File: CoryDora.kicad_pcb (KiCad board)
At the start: 2 copper layers, 89.6 x 60.1 mm, 26 parts, among them J1 OLED_128x32, SW1 RotaryEncoder_Switch, U1 RP2040_Zero

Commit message: chore: made modifications for v1.1
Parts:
- added G***: LOGO, DEKU_logo:DEKU_logo, B.Cu at (158.9, 116.1)
- moved SW1 1.60 mm to (147.3, 133.1)
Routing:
- net ENCODER_SW: track 43.3 -> 49.9 mm
- net ENCODER_A: track 36.9 -> 38.6 mm
- net GND: track 63.1 -> 64.7 mm
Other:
- board text added: "CoryDora v1.1"
- board text added: "S8"
- board text removed: "CoryDora v1"

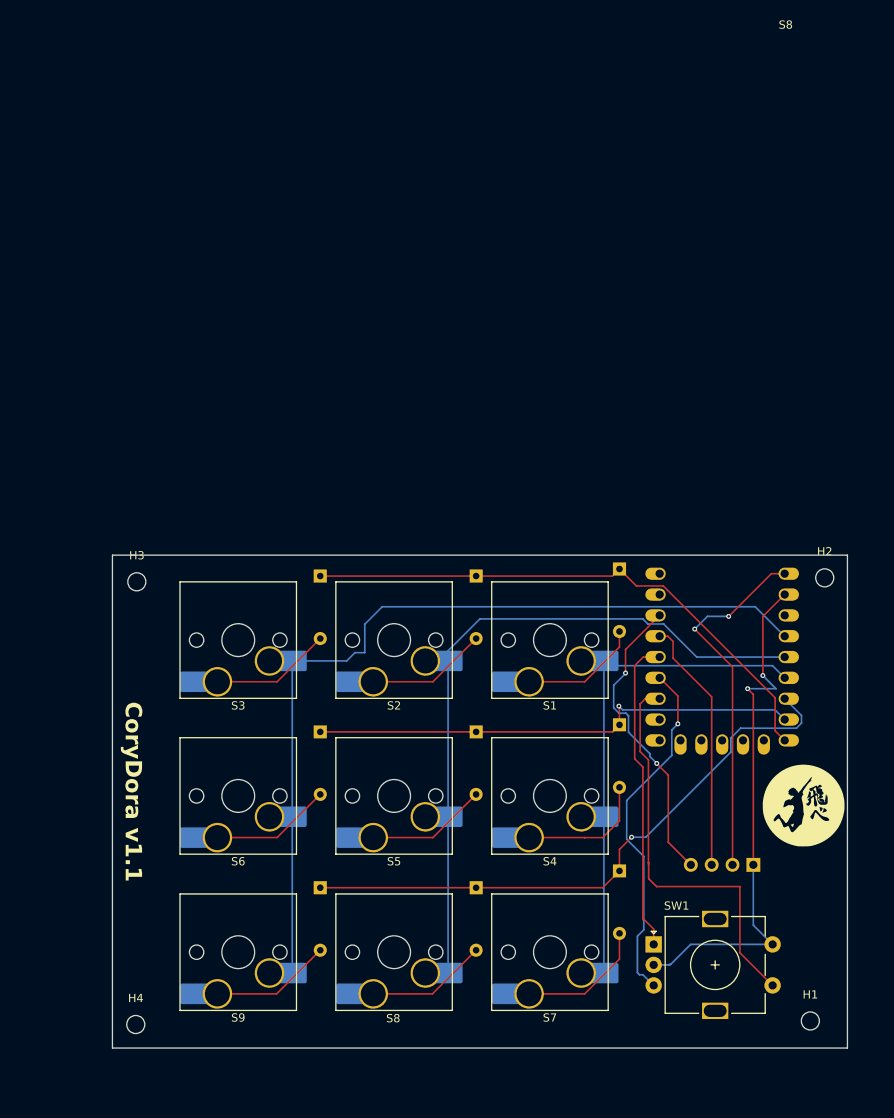
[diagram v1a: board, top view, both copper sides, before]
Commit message: chore: added front and bottom copper fill
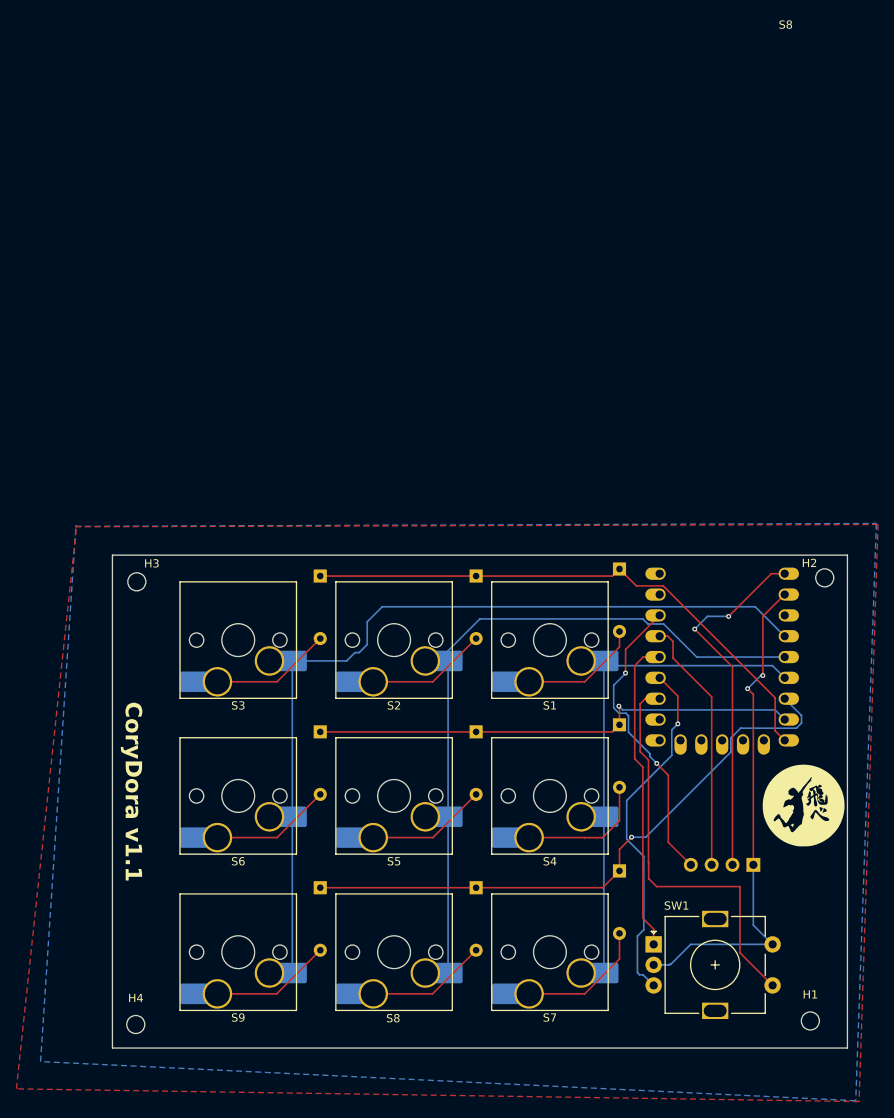
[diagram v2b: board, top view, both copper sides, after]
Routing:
- net GND: track 64.7 -> 61.5 mm
- added copper zone on B.Cu, net (none)
- added copper zone on F.Cu, net (none)
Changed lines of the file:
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@@
 			(psnegative no)
 			(psa4output no)
-			(plotreference yes)
+			(plotreference no)
 			(plotvalue no)
 			(plotfptext yes)
 			(plotinvisibletext no)
 			(sketchpadsonfab no)
-			(subtractmaskfromsilk yes)
+			(subtractmaskfromsilk no)
 			(outputformat 1)
 			(mirror no)
@@
 	(net 21 "ENCODER_B")
 	(net 22 "ENCODER_SW")
-	(net 23 "unconnected-(U1-7-Pad8)")
-	(net 24 "unconnected-(U1-12-Pad13)")
-	(net 25 "unconnected-(U1-13-Pad14)")
-	(net 26 "unconnected-(U1-0-Pad1)")
-	(net 27 "unconnected-(U1-10-Pad11)")
-	(net 28 "unconnected-(U1-11-Pad12)")
-	(net 29 "unconnected-(U1-1-Pad2)")
-	(net 30 "unconnected-(U1-3V3-Pad21)")
-	(net 31 "unconnected-(U1-8-Pad9)")
-	(net 32 "unconnected-(U1-9-Pad10)")
+	(net 23 "unconnected-(U1-9-Pad10)")
+	(net 24 "unconnected-(U1-8-Pad9)")
+	(net 25 "unconnected-(U1-3V3-Pad21)")
+	(net 26 "unconnected-(U1-1-Pad2)")
+	(net 27 "unconnected-(U1-11-Pad12)")
+	(net 28 "unconnected-(U1-10-Pad11)")
+	(net 29 "unconnected-(U1-0-Pad1)")
+	(net 30 "unconnected-(U1-13-Pad14)")
+	(net 31 "unconnected-(U1-12-Pad13)")
+	(net 32 "unconnected-(U1-7-Pad8)")
 	(footprint "Downloads:12"
 		(layer "F.Cu")
@@
 			)
 		)
+		(model "${MY_LIBRARY}/11mm-metal-shaft-rotary-encoders-tht-vertical-w-push-on-switch-1.snapshot.2/models3d/Encoders/EC11-THT-15F-green.step"
+			(offset
+				(xyz 7.5 -2.5 -0.25)
+			)
+			(scale
+				(xyz 1 1 1)
+			)
+			(rotate
+				(xyz 180 180 -90)
+			)
+		)
 	)
 	(footprint "ScottoKeebs_Hotswap:Hotswap_MX_Plated_1.00u"
@@
 		(tags "mounting hole 2.2mm no annular m2")
 		(property "Reference" "H3"
-			(at 0 -3.2 0)
+			(at 1.8288 -2.2098 0)
 			(layer "F.SilkS")
 			(effects
@@
 			(at 5.75 5.75 -90)
 			(layer "F.Fab")
-			(hide yes)
 			(effects
 				(font
@@
 		(tags "mounting hole 2.2mm no annular m2")
 		(property "Reference" "H2"
-			(at 0 -3.2 0)
+			(at -1.8542 -1.778 0)
 			(layer "F.SilkS")
 			(effects
@@
 		)
 		(property "Value" "RP2040_Zero"
-			(at -16.8434 5.54718 180)
+			(at -10.344 1.349891 -90)
 			(layer "B.SilkS")
-			(hide yes)
 			(effects
 				(font
@@
 			(layers "*.Cu" "*.Mask")
 			(remove_unused_layers no)
-			(net 26 "unconnected-(U1-0-Pad1)")
+			(net 29 "unconnected-(U1-0-Pad1)")
 			(pinfunction "0")
 			(pintype "bidirectional+no_connect")
@@
 			(layers "*.Cu" "*.Mask")
 			(remove_unused_layers no)
-			(net 29 "unconnected-(U1-1-Pad2)")
+			(net 26 "unconnected-(U1-1-Pad2)")
 			(pinfunction "1")
 			(pintype "bidirectional+no_connect")
@@
 			(layers "*.Cu" "*.Mask")
 			(remove_unused_layers no)
-			(net 23 "unconnected-(U1-7-Pad8)")
+			(net 32 "unconnected-(U1-7-Pad8)")
 			(pinfunction "7")
 			(pintype "bidirectional+no_connect")
@@
 			(layers "*.Cu" "*.Mask")
 			(remove_unused_layers no)
-			(net 31 "unconnected-(U1-8-Pad9)")
+			(net 24 "unconnected-(U1-8-Pad9)")
 			(pinfunction "8")
 			(pintype "bidirectional+no_connect")
@@
 			(layers "*.Cu" "*.Mask")
 			(remove_unused_layers no)
-			(net 32 "unconnected-(U1-9-Pad10)")
+			(net 23 "unconnected-(U1-9-Pad10)")
 			(pinfunction "9")
 			(pintype "bidirectional+no_connect")
@@
 			(layers "*.Cu" "*.Mask")
 			(remove_unused_layers no)
-			(net 27 "unconnected-(U1-10-Pad11)")
+			(net 28 "unconnected-(U1-10-Pad11)")
 			(pinfunction "10")
 			(pintype "bidirectional+no_connect")
@@
 			(layers "*.Cu" "*.Mask")
 			(remove_unused_layers no)
-			(net 28 "unconnected-(U1-11-Pad12)")
+			(net 27 "unconnected-(U1-11-Pad12)")
 			(pinfunction "11")
 			(pintype "bidirectional+no_connect")
@@
 			(layers "*.Cu" "*.Mask")
 			(remove_unused_layers no)
-			(net 24 "unconnected-(U1-12-Pad13)")
+			(net 31 "unconnected-(U1-12-Pad13)")
 			(pinfunction "12")
 			(pintype "bidirectional+no_connect")
@@
 			(layers "*.Cu" "*.Mask")
 			(remove_unused_layers no)
-			(net 25 "unconnected-(U1-13-Pad14)")
+			(net 30 "unconnected-(U1-13-Pad14)")
 			(pinfunction "13")
 			(pintype "bidirectional+no_connect")
@@
 			(layers "*.Cu" "*.Mask")
 			(remove_unused_layers no)
-			(net 30 "unconnected-(U1-3V3-Pad21)")
+			(net 25 "unconnected-(U1-3V3-Pad21)")
 			(pinfunction "3V3")
 			(pintype "power_out+no_connect")
@@
 	)
 	(segment
-		(start 162.2044 101.904262)
-		(end 160.6042 100.304062)
-		(width 0.2)
-		(layer "B.Cu")
-		(net 16)
-	)
-	(segment
-		(start 158.75 101.904262)
-		(end 162.2044 101.904262)
+		(start 160.6042 100.304062)
+		(end 160.3502 100.304062)
 		(width 0.2)
 		(layer "B.Cu")
@@
 	)
 	(segment
+		(start 160.3502 100.304062)
+		(end 158.75 101.904262)
+		(width 0.2)
+		(layer "B.Cu")
+		(net 16)
+	)
+	(segment
 		(start 149.15 135.583462)
 		(end 147.2934 135.583462)
@@
 	)
 	(segment
-		(start 114.203309 91.917153)
-		(end 159.675 91.917153)
+		(start 112.3696 93.750862)
+		(end 112.3696 96.519462)
 		(width 0.2)
 		(layer "B.Cu")
@@
 	)
 	(segment
-		(start 159.675 91.917153)
-		(end 163.265 95.507153)
+		(start 103.23 117.523262)
+		(end 103.23 136.573262)
 		(width 0.2)
 		(layer "B.Cu")
@@
 	)
 	(segment
-		(start 112.0648 94.055662)
-		(end 114.203309 91.917153)
+		(start 103.23 98.523262)
+		(end 109.8578 98.523262)
+		(width 0.2)
+		(layer "B.Cu")
+		(net 19)
+	)
+	(segment
+		(start 114.203309 91.917153)
+		(end 159.675 91.917153)
 		(width 0.2)
 		(layer "B.Cu")
@@
 	)
 	(segment
-		(start 103.23 117.523262)
-		(end 103.23 136.573262)
+		(start 112.3696 96.519462)
+		(end 111.379 97.510062)
 		(width 0.2)
 		(layer "B.Cu")
@@
 	)
 	(segment
-		(start 110.871 97.510062)
-		(end 112.0648 97.510062)
+		(start 159.675 91.917153)
+		(end 163.265 95.507153)
 		(width 0.2)
 		(layer "B.Cu")
@@
 	)
 	(segment
-		(start 103.23 98.523262)
-		(end 109.8578 98.523262)
+		(start 110.871 97.510062)
+		(end 111.379 97.510062)
 		(width 0.2)
 		(layer "B.Cu")
@@
 	)
 	(segment
-		(start 112.0648 97.510062)
-		(end 112.0648 94.055662)
+		(start 112.3696 93.750862)
+		(end 114.203309 91.917153)
 		(width 0.2)
 		(layer "B.Cu")
@@
 	)
 	(segment
-		(start 145.975 130.063262)
+		(start 147.2934 131.213462)
 		(end 145.975 129.895062)
 		(width 0.2)
@@
 	)
 	(segment
-		(start 145.975 129.895062)
-		(end 147.2934 131.213462)
-		(width 0.2)
-		(layer "F.Cu")
-		(net 20)
-	)
-	(segment
 		(start 145.975 111.455862)
 		(end 144.9832 110.464062)
@@
 	)
 	(segment
-		(start 146.685 123.113262)
-		(end 146.6596 123.087862)
-		(width 0.2)
-		(layer "F.Cu")
-		(net 22)
-	)
-	(segment
 		(start 146.274909 103.127153)
 		(end 148.025 103.127153)
@@
 	)
 	(segment
-		(start 157.8102 126.034262)
-		(end 147.6502 126.034262)
+		(start 146.685 123.113262)
+		(end 146.6596 123.087862)
 		(width 0.2)
 		(layer "F.Cu")
@@
 	)
 	(segment
-		(start 146.6596 123.347862)
-		(end 146.6596 123.087862)
+		(start 157.8102 126.034262)
+		(end 147.6502 126.034262)
 		(width 0.2)
 		(layer "F.Cu")
@@
 		(net 22)
 	)
+	(zone
+		(net 0)
+		(net_name "")
+		(layer "F.Cu")
+		(hatch edge 0.5)
+		(connect_pads
+			(clearance 0.5)
+		)
+		(min_thickness 0.25)
+		(filled_areas_thickness no)
+		(fill yes
+			(thermal_gap 0.5)
+			(thermal_bridge_width 0.5)
+			(island_removal_mode 1)
+			(island_area_min 10)
+		)
+		(polygon
+			(pts
+				(xy 76.7588 82.168462) (xy 174.6504 81.889062) (xy 172.339 152.247062) (xy 69.596 150.697662) (xy 76.9366 82.066862)
+			)
+		)
+	)
+	(zone
+		(net 0)
+		(net_name "")
+		(layer "B.Cu")
+		(hatch edge 0.5)
+		(priority 1)
+		(connect_pads
+			(clearance 0.5)
+		)
+		(min_thickness 0.25)
+		(filled_areas_thickness no)
+		(fill yes
+			(thermal_gap 0.5)
+			(thermal_bridge_width 0.5)
+			(island_removal_mode 1)
+			(island_area_min 10)
+		)
+		(polygon
+			(pts
+				(xy 76.8096 82.117662) (xy 174.4472 81.762062) (xy 171.9326 152.145462) (xy 72.5424 147.370262)
+				(xy 76.8604 81.990662)
+			)
+		)
+	)
 )

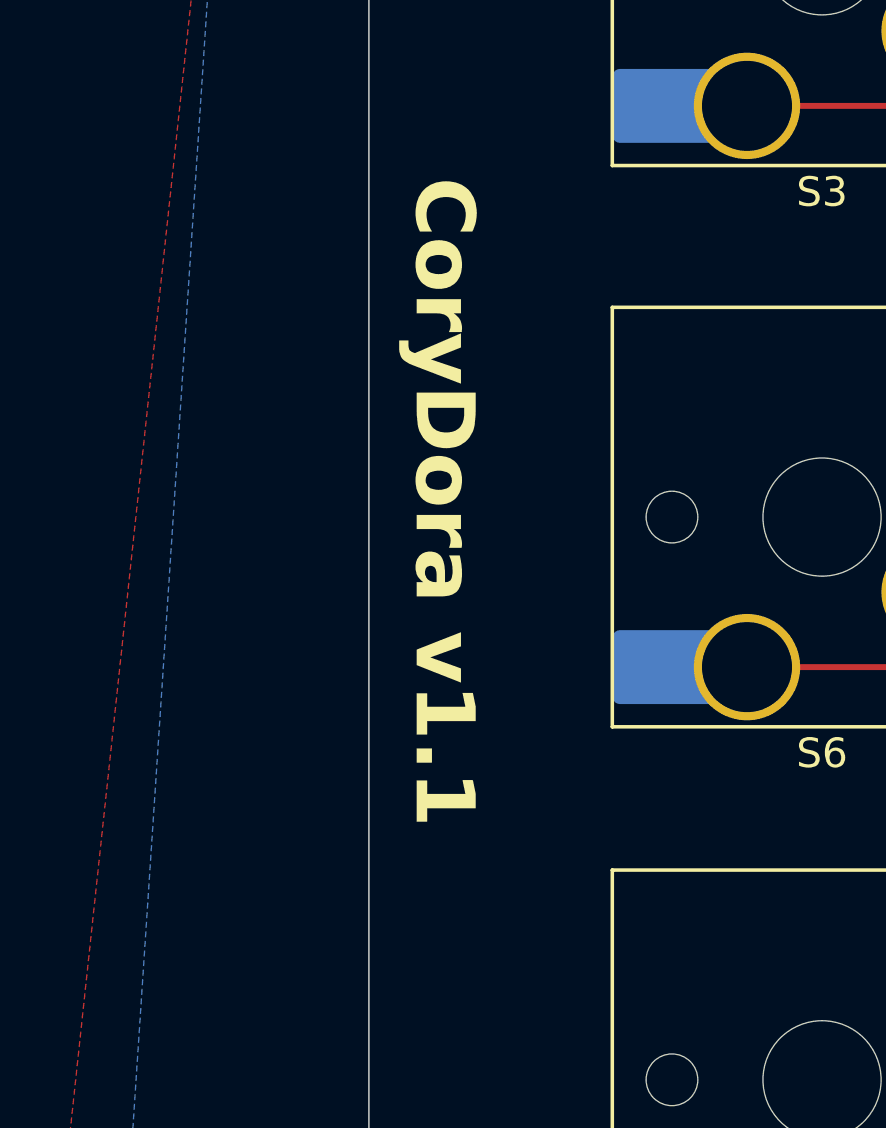
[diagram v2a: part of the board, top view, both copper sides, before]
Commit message: feat: added v1.2 case design
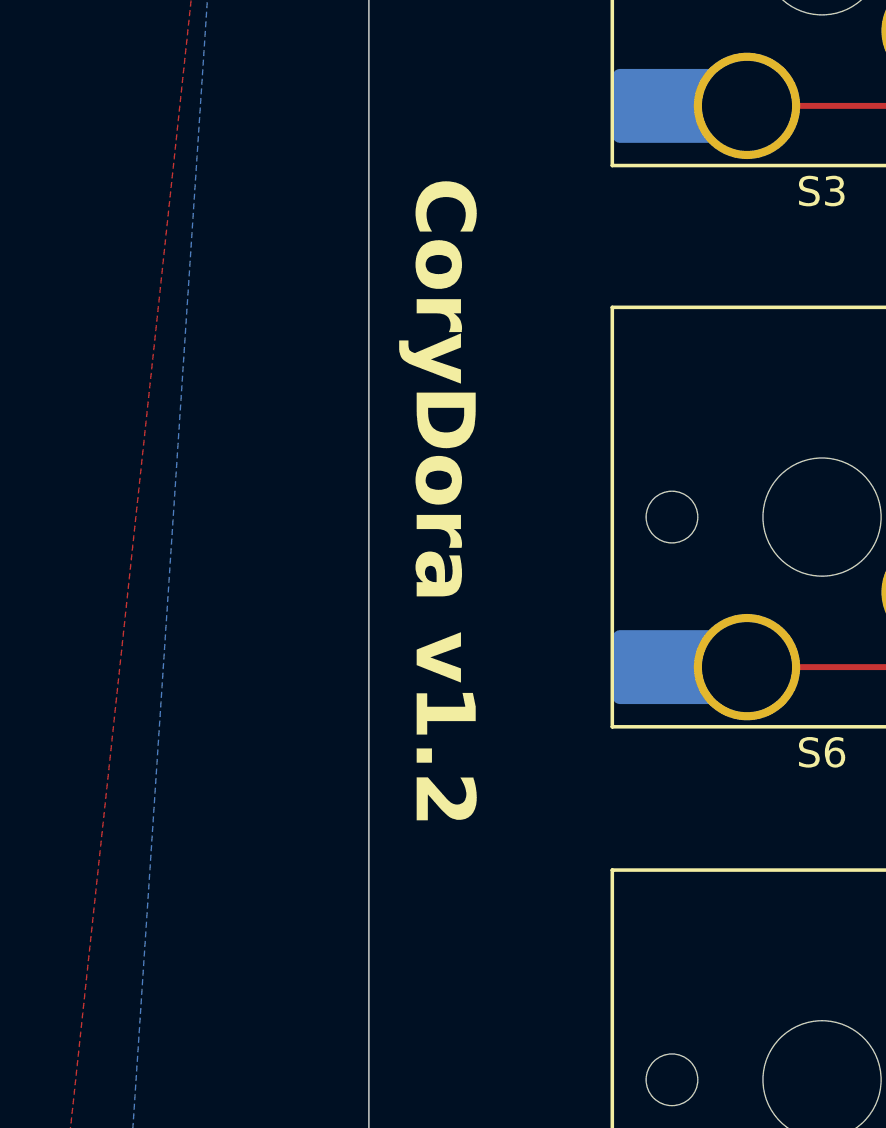
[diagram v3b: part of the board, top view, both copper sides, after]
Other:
- board text added: "CoryDora v1.2"
- board text removed: "CoryDora v1.1"
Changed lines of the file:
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@@
 			(plotreference no)
 			(plotvalue no)
-			(plotfptext yes)
+			(plotfptext no)
 			(plotinvisibletext no)
 			(sketchpadsonfab no)
@@
 			)
 		)
-		(property "Description" "Push button switch, normally open, two pins, 45Â° tilted"
+		(property "Description" "Push button switch, normally open, two pins, 45° tilted"
 			(at 0 0 180)
 			(unlocked yes)
@@
 			)
 		)
-		(property "Description" "Push button switch, normally open, two pins, 45Â° tilted"
+		(property "Description" "Push button switch, normally open, two pins, 45° tilted"
 			(at 0 0 180)
 			(unlocked yes)
@@
 			)
 		)
-		(property "Description" "Push button switch, normally open, two pins, 45Â° tilted"
+		(property "Description" "Push button switch, normally open, two pins, 45° tilted"
 			(at 0 0 180)
 			(unlocked yes)
@@
 			)
 		)
-		(property "Description" "Push button switch, normally open, two pins, 45Â° tilted"
+		(property "Description" "Push button switch, normally open, two pins, 45° tilted"
 			(at 0 0 180)
 			(unlocked yes)
@@
 			)
 		)
-		(property "Description" "Push button switch, normally open, two pins, 45Â° tilted"
+		(property "Description" "Push button switch, normally open, two pins, 45° tilted"
 			(at 0 0 180)
 			(unlocked yes)
@@
 			)
 		)
-		(property "Description" "Push button switch, normally open, two pins, 45Â° tilted"
+		(property "Description" "Push button switch, normally open, two pins, 45° tilted"
 			(at 0 0 180)
 			(unlocked yes)
@@
 			)
 		)
-		(property "Description" "Push button switch, normally open, two pins, 45Â° tilted"
+		(property "Description" "Push button switch, normally open, two pins, 45° tilted"
 			(at 0 0 180)
 			(unlocked yes)
@@
 			)
 		)
-		(property "Description" "Push button switch, normally open, two pins, 45Â° tilted"
+		(property "Description" "Push button switch, normally open, two pins, 45° tilted"
 			(at 0 0 180)
 			(unlocked yes)
@@
 			)
 		)
-		(property "Description" "Push button switch, normally open, two pins, 45Â° tilted"
+		(property "Description" "Push button switch, normally open, two pins, 45° tilted"
 			(at 0 0 180)
 			(unlocked yes)
@@
 		)
 		(property "Footprint" "DEKU_logo:DEKU_logo"
-			(at 0 0 0)
+			(at 5 0.5 0)
 			(layer "B.Fab")
 			(hide yes)
@@
 			(at -10.344 1.349891 -90)
 			(layer "B.SilkS")
+			(hide yes)
 			(effects
 				(font
@@
 		)
 	)
-	(gr_text "CoryDora v1.1"
+	(gr_text "CoryDora v1.2"
 		(at 82.677 103.479062 270)
 		(layer "F.SilkS")

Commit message: chore: modified readme
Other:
- board text added: "{dblquote}I don't want to believe. I want to know.{dblquote} - Carl Sagan"
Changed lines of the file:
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@@
 		(layer "Edge.Cuts")
+	)
+	(gr_text "{dblquote}I don't want to believe. I want to know.{dblquote} - Carl Sagan"
+		(at 152.4216 144.136462 0)
+		(layer "B.SilkS")
+		(effects
+			(font
+				(size 1.5 1.5)
+				(thickness 0.3)
+				(bold yes)
+			)
+			(justify left bottom mirror)
+		)
 	)
 	(gr_text "S8"
